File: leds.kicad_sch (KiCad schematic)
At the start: 40 parts, among them J3 Conn_01x10_Female, J4 Conn_01x10_Male, J5 Conn_01x10_Male, J6 Conn_01x10_Female

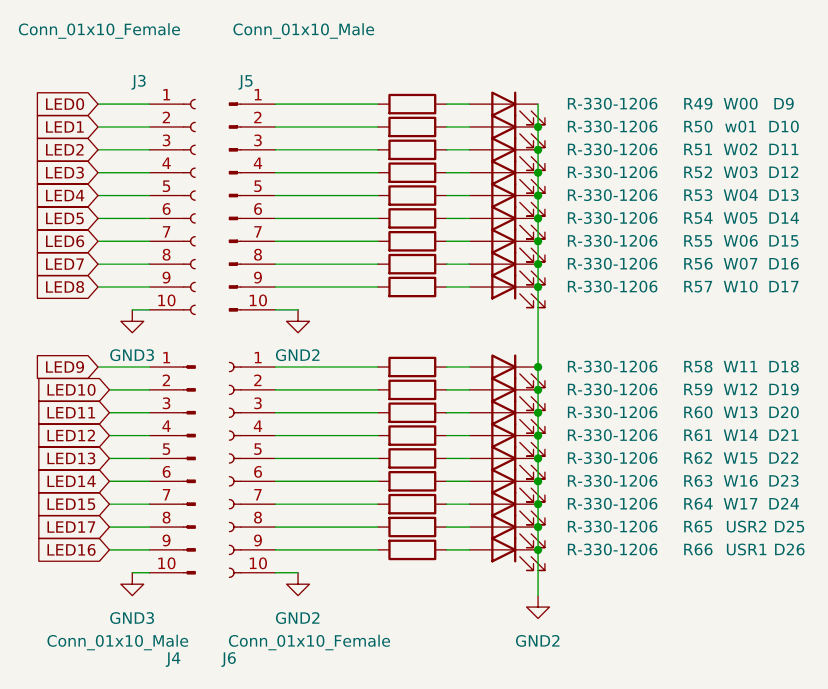
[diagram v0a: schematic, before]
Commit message: Changed all R to 0603
all res to 0603 and changed JACK to LED Jack (for fancy)
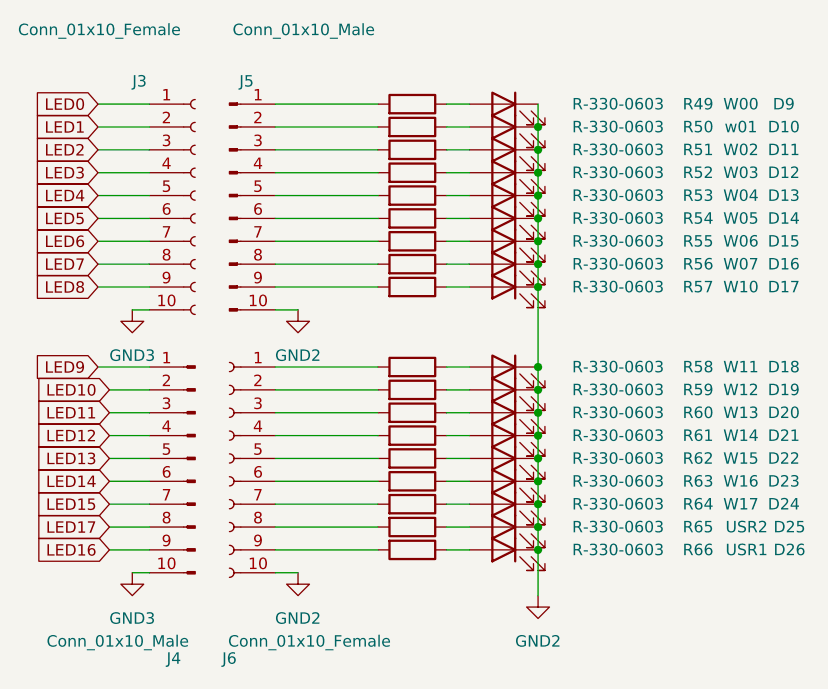
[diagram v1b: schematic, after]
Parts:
- R49, R50, R51, R52, R53, R54, R55, R56, R57, R58, R59, R60, R61, R62, R63, R64, R65, R66: value R-330-1206 -> R-330-0603; footprint Resistor_SMD:R_1206_3216Metric_Pad1.30x1.75mm_HandSolder -> Resistor_SMD:R_0603_1608Metric_Pad0.98x0.95mm_HandSolder; symbol eurorack:R-330-1206 -> eurorack:R-330-0603; P 250mW -> 0.1W
